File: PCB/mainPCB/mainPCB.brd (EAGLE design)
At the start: 98.7 x 80 mm, 58 parts, among them CN1 SDS-50J, CN2 SDS-50J, CN3 SDS-50J, CN4 SDS-50J, J2 RASPBERRYPI-40-PIN-GPIO, T2 BC817, T3 BC817, T4 BC817, T6 BC817, U1 AT24C256C-SSHL-B, U11 SFH615A-07, U12 ALQ105, U3 SFH615A-07, U4 ALQ105, U5 SFH615A-07, U6 ALQ105, U7 SFH615A-07, U8 ALQ105

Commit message: Adding files for v0.2
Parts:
- removed J1, J3, J4, J5: (no value), SparkFun-Connectors:1X02_2.54_SCREWTERM
- removed U$1: MCP3208I/SL, adcLib:SO-16DW
- added C10, C11, C2, C3, C4, C5, C6, C7, C8, C9: 0.1uF, SparkFun-Capacitors:0603-CAP
- added C12, C13: 10uF, SparkFun-Capacitors:1206-CAP
- added C14, C15: EEE-HA1C471UPCAP_PAN_EEE_F-L, EEE-HA1C471UP:CAP_PAN_EEE_F-L
- added CN5, CN6, CN7, CN8: SDS-50J, SDS-50J:SDS-50J
- added CON1: 1776244-4, lib:1776244-4
- added D10, D11, D5, D8, D9: (no value), SparkFun-DiscreteSemi:SMA-DIODE
- added F5, F6, F7, F8: 3544-2, lib:3544-2
- added FRAME3: FRAME-LETTER, SparkFun-Aesthetics:CREATIVE_COMMONS
- added Q1: DMMT5401-7-F, DMMT5401-7-F:SOT26
- added R24: 0, SparkFun-Passives:1206
- added R25, R40, R43, R46, R49: 10k, SparkFun-Passives:0603-RES
- added R26, R41, R44, R47, R50: 47k, SparkFun-Passives:0603-RES
- added R27: DNP, SparkFun-Passives:1206
- added R28, R29, R30, R31, R32, R33, R34, R35: 330, SparkFun-Passives:0603-RES
- added R39, R42, R45, R48: 47, SparkFun-Passives:0603-RES
- added T5, T7, T8, T9: BC817, lib:BC817
- added U$2: MCP3208T-CI/SL, MCP3208T-CI_SL:SOIC16-N_MC
- added U13, U15, U17, U19: SFH615A-07, lib:SFH615A-07
- added U14, U16, U18, U20: ALQ105, lib:ALQ105
- added U2: DMG2305UX-13SOT-23-M, DMG2359UX:SOT-23-M
- R14, R15: device SparkFun-Passives:0603-RES -> SparkFun-Passives:1206
- R21: value 1k -> 3.9k
- moved FRAME2 73.1 mm to (171.1, 3.12)
- moved FRAME1 67.6 mm to (165.7, 3.12)
- moved R20 54.6 mm to (93.4, 11.8), turned to 270 degrees
- moved R14 44.5 mm to (112.8, 2.92), flipped to the top, turned to 180 degrees
- moved R19 34.3 mm to (76.5, 12.6)
- moved U12 18.3 mm to (77.5, 54.6)
- moved U6 17.4 mm to (54.6, 54.6)
- moved U8 16.6 mm to (31.8, 54.6)
- moved U4 15.9 mm to (8.89, 54.6)
- moved R15 13.7 mm to (58.0, 17.0), turned to 270 degrees
- moved R2 13.3 mm to (39.9, 25.9)
- moved R7 13.1 mm to (47.8, 26.6)
- moved R1 13.0 mm to (37.0, 27.8)
- moved R13 12.8 mm to (34.0, 29.7)
- moved R23 11.3 mm to (10.1, 26.8)
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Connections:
- new net 5V_RPI: C12.1, C13.1, Q1.6, R14.1, R27.1, U2.3
- new net A1_F: C2.1, CN1.2, R28.2
- new net A2_F: C3.1, CN2.2, R29.2
- new net A3_F: C4.1, CN3.2, R30.2
- new net A4_F: C5.1, CN4.2, R31.2
- new net A5_F: C6.1, CN5.2, R32.2
- new net A6_F: C7.1, CN6.2, R33.2
- new net A7_F: C8.1, CN7.2, R34.2
- new net A8_F: C9.1, CN8.2, R35.2
- new net N$29: Q1.4, R26.2, U2.1
- new net N$30: CON1.4, D5.A
- new net N$31: F5.P$1, F5.P$2, U14.P$3
- new net N$32: F6.P$1, F6.P$2, U16.P$3
- new net N$33: F7.P$1, F7.P$2, U20.P$3
- new net N$34: F8.P$1, F8.P$2, U18.P$3
- new net N$35: R39.2, U13.P$1
- new net N$36: C10.1, C11.1, R19.1, U$2.15, U$2.16
- new net N$37: R40.2, U13.P$3
- new net N$38: R40.1, R41.2, T5.P$2
- new net N$39: D8.A, T5.P$1, U14.P$2
- new net N$40: R42.2, U15.P$1
- new net N$41: R43.2, U15.P$3
- new net N$42: R43.1, R44.2, T7.P$2
- new net N$43: D9.A, T7.P$1, U16.P$2
- new net N$44: R45.2, U17.P$1
- new net N$45: R46.2, U17.P$3
- new net N$46: R46.1, R47.2, T8.P$2
- new net N$47: D10.A, T8.P$1, U18.P$2
- new net N$48: R48.2, U19.P$1
- new net N$49: R49.2, U19.P$3
- new net N$50: R49.1, R50.2, T9.P$2
- new net N$51: D11.A, T9.P$1, U20.P$2
- new net R5: CN5.5, U14.P$4
- new net R6: CN6.5, U16.P$4
- new net R7: CN7.5, U20.P$4
- new net R8: CN8.5, U18.P$4
- new net RELAY5: J2.13, R39.1
- new net RELAY6: J2.15, R42.1
- new net RELAY7: J2.29, R48.1
- new net RELAY8: J2.31, R45.1
- net 12V: now also D5.C, F5.P$3, F5.P$4, F6.P$3, F6.P$4, F7.P$3, F7.P$4, F8.P$3, F8.P$4; no longer J4.P1, J4.P2
- net 3_3V: no longer J1.P1, J1.P2, U$1.15
- net 5V: now also C14.1, C15.1, CN5.1, CN6.1, CN7.1, CN8.1, CON1.1, D10.C, D11.C, D8.C, D9.C, Q1.5, R27.2, U12.P$1, U13.P$4, U14.P$1, U15.P$4, U16.P$1, U17.P$4, U18.P$1, U19.P$4, U2.2, U20.P$1, U4.P$1, U6.P$1, U8.P$1; no longer J3.P1, J3.P2, R14.1, U12.P$2, U4.P$2, U6.P$2, U8.P$2
- net A1: now also R28.1, U$2.1; no longer CN1.2, U$1.1
- net A2: now also R29.1, U$2.2; no longer CN2.2, U$1.2
- net A3: now also R30.1, U$2.3; no longer CN3.2, U$1.3
- net A4: now also R31.1, U$2.4; no longer CN4.2, U$1.4
- net A5: now also R32.1, U$2.5; no longer U$1.5
- net A6: now also R33.1, U$2.6; no longer U$1.6
- net A7: now also R34.1, U$2.7; no longer U$1.7
- net A8: now also R35.1, U$2.8; no longer U$1.8
- net AGND: now also U$2.14; no longer U$1.14
- net CLK: now also U$2.13; no longer U$1.13
- net COM: now also CN5.3, CN6.3, CN7.3, CN8.3, R24.1
- net CS_ADC: now also U$2.10; no longer U$1.10
- net GND: now also C10.2, C11.2, C12.2, C13.2, C14.2, C15.2, C2.2, C3.2, C4.2, C5.2, C6.2, C7.2, C8.2, C9.2, CN5.4, CN6.4, CN7.4, CN8.4, CON1.2, CON1.3, R24.2, R25.1, R26.1, R41.1, R44.1, R47.1, R50.1, T5.P$3, T7.P$3, T8.P$3, T9.P$3, U$2.9, U13.P$2, U15.P$2, U17.P$2, U19.P$2; no longer J5.P1, J5.P2, U$1.9
- net MISO: now also U$2.12; no longer U$1.12
- net MOSI: now also U$2.11; no longer U$1.11
- net N$12: now also U6.P$2; no longer U6.P$1
- net N$16: now also U8.P$2; no longer U8.P$1
- net N$24: now also U12.P$2; no longer U12.P$1
- net N$27: now also Q1.1, Q1.2, Q1.3, R25.2; no longer R19.1, U$1.16
- net N$8: now also U4.P$2; no longer U4.P$1
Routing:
- net 5V: track 314.2 -> 578.8 mm
- net RELAY8: track 0.00 -> 168.2 mm, vias 0 -> 3
- net A8_F: track 0.00 -> 150.4 mm
- net COM: track 86.5 -> 230.3 mm
- net RELAY7: track 0.00 -> 139.7 mm, vias 0 -> 3
- net A7_F: track 0.00 -> 133.3 mm
- net GND: track 208.1 -> 78.9 mm, vias 9 -> 78
- net A1_F: track 0.00 -> 114.3 mm
- net A6_F: track 0.00 -> 104.7 mm
- net 12V: track 141.7 -> 233.5 mm
- net A2_F: track 0.00 -> 91.1 mm
- net RELAY6: track 0.00 -> 90.9 mm, vias 0 -> 1
- net A5_F: track 0.00 -> 81.2 mm
- net A1: track 80.4 -> 3.69 mm
- net A3_F: track 0.00 -> 74.4 mm
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- removed copper zone on layer 16, net AGND
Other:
- board size 98.7 x 80 mm -> 187 x 85 mm
- board text added: "v0.2"
- board text removed: "3.3V"
- board text removed: "v0.1"

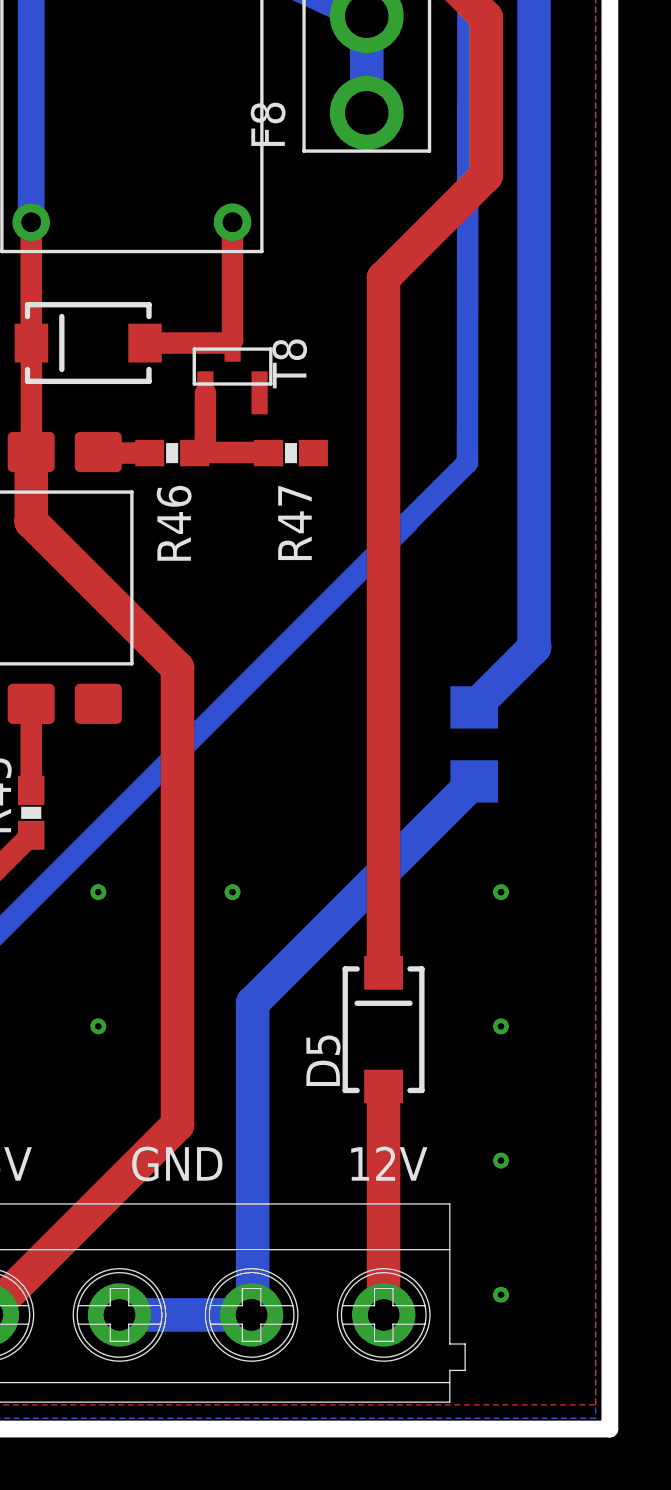
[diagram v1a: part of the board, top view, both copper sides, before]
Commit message: Removed Diode.
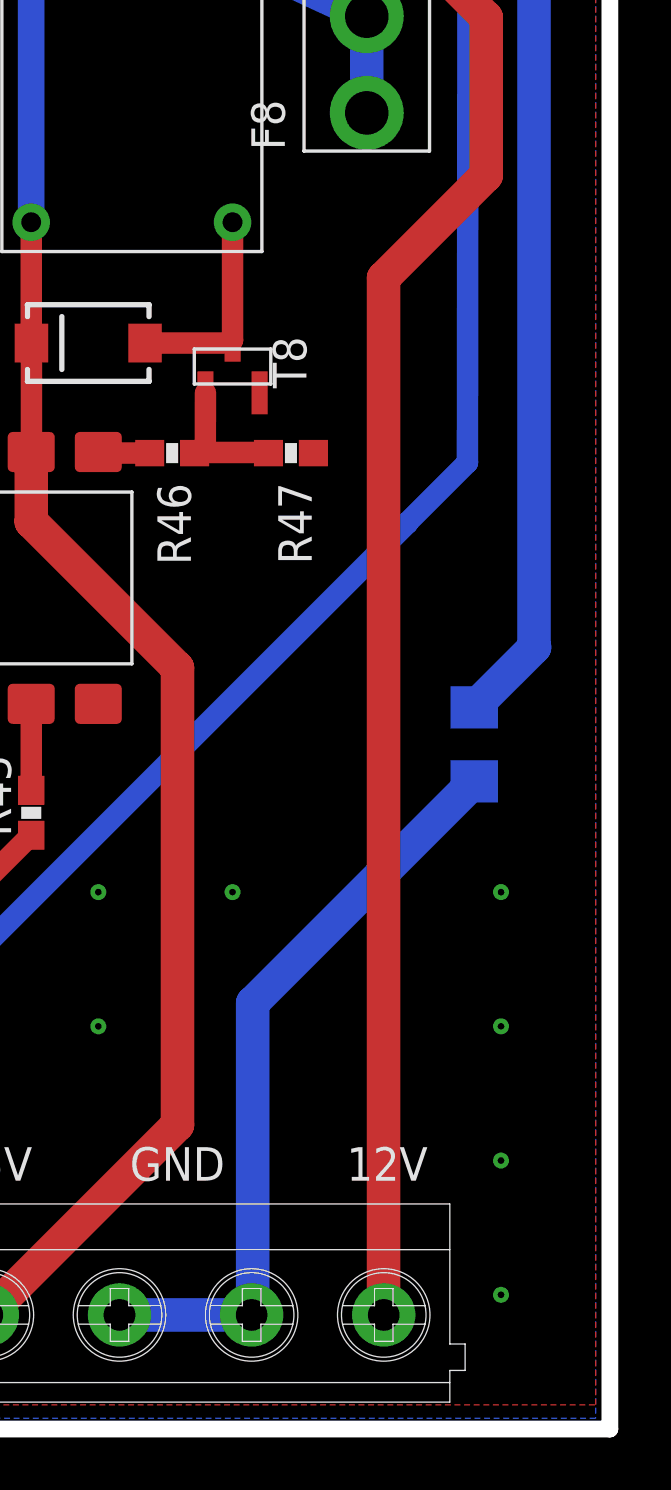
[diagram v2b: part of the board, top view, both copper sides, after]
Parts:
- removed D5: (no value), SparkFun-DiscreteSemi:SMA-DIODE
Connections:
- removed net N$30: CON1.4, D5.A
- net 12V: now also CON1.4; no longer D5.C
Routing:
- net 12V: track 233.5 -> 246.4 mm
- net N$30: track 8.65 -> 0.00 mm
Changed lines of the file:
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@@
 <?xml version="1.0" encoding="utf-8"?>
 <!DOCTYPE eagle SYSTEM "eagle.dtd">
-<eagle version="8.4.3">
+<eagle version="8.3.2">
 <drawing>
 <settings>
@@
 <setting verticaltext="up"/>
 </settings>
-<grid distance="0.127" unitdist="mm" unit="mm" style="dots" multiple="1" display="yes" altdistance="0.127" altunitdist="mm" altunit="mm"/>
+<grid distance="0.127" unitdist="mm" unit="mil" style="dots" multiple="1" display="yes" altdistance="0.127" altunitdist="mm" altunit="mil"/>
 <layers>
 <layer number="1" name="Top" color="4" fill="1" visible="yes" active="yes"/>
@@
 <param name="dpMaxLengthDifference" value="10mm"/>
 <param name="dpGapFactor" value="2.5"/>
+<param name="checkGrid" value="0"/>
 <param name="checkAngle" value="0"/>
 <param name="checkFont" value="1"/>
 <param name="checkRestrict" value="1"/>
-<param name="checkStop" value="0"/>
 <param name="useDiameter" value="13"/>
 <param name="maxErrors" value="50"/>
@@
 <attribute name="NAME" x="97.536" y="18.288" size="1.27" layer="26" font="vector" rot="MR180"/>
 <attribute name="PROD_ID" value="CAP-00810" x="95.885" y="17.78" size="1.778" layer="28" rot="MR180" display="off"/>
-</element>
-<element name="D5" library="SparkFun-DiscreteSemi" package="SMA-DIODE" value="" x="178.435" y="15.113" smashed="yes" rot="R90">
-<attribute name="NAME" x="176.784" y="12.827" size="1.27" layer="25" rot="R90"/>
-<attribute name="VALUE" x="176.784" y="15.367" size="0.4064" layer="27" rot="R90"/>
 </element>
 <element name="FRAME3" library="SparkFun-Aesthetics" package="CREATIVE_COMMONS" value="FRAME-LETTER" x="176.276" y="3.1242" smashed="yes"/>
@@
 <contactref element="F4" pad="P$4"/>
 <contactref element="F4" pad="P$3"/>
-<contactref element="D5" pad="C"/>
 <contactref element="F5" pad="P$4"/>
 <contactref element="F5" pad="P$3"/>
@@
 <wire x1="63.5" y1="57.94" x2="63.5" y2="61.6" width="1.27" layer="1"/>
 <wire x1="182.3212" y1="53.4188" x2="177.8" y2="57.94" width="1.27" layer="1"/>
-<wire x1="178.435" y1="17.263" x2="178.435" y2="43.561" width="1.27" layer="1"/>
-<wire x1="178.435" y1="43.561" x2="182.3212" y2="47.4472" width="1.27" layer="1"/>
+<wire x1="182.3212" y1="47.4472" x2="178.435" y2="43.561" width="1.27" layer="1"/>
 <wire x1="182.3212" y1="47.4472" x2="182.3212" y2="53.4188" width="1.27" layer="1"/>
+<contactref element="CON1" pad="4"/>
+<wire x1="178.435" y1="4.325" x2="178.442" y2="4.318" width="1.27" layer="1"/>
+<wire x1="178.435" y1="43.561" x2="178.435" y2="4.325" width="1.27" layer="1"/>
 </signal>
 <signal name="3.3V">
@@
 <wire x1="23.241" y1="60.833" x2="23.241" y2="40.1574" width="0.8128" layer="16"/>
 </signal>
-<signal name="N$30">
-<contactref element="CON1" pad="4"/>
-<contactref element="D5" pad="A"/>
-<wire x1="178.435" y1="12.963" x2="178.435" y2="4.325" width="1.27" layer="1"/>
-<wire x1="178.435" y1="4.325" x2="178.442" y2="4.318" width="1.27" layer="1"/>
-</signal>
 <signal name="5V_RPI" class="3">

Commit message: Adding files
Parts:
- added D1, D12, D13, D14, D15, D16, D5, D7: BAV99-7-F, SparkFun-DiscreteSemi:SOT23-3
- added F9: 3544-2, lib:3544-2
- moved R24 6.25 mm to (184.2, 31.7)
- moved C14 1.27 mm to (147.4, 13.8)
- moved C15 1.27 mm to (158.9, 13.8)
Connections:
- new net N$28: CON1.4, F9.P$1, F9.P$2
- net 12V: now also F9.P$3, F9.P$4; no longer CON1.4
- net 5V: now also D1.2, D12.2, D13.2, D14.2, D15.2, D16.2, D5.2, D7.2
- net A1_F: now also D1.3
- net A2_F: now also D5.3
- net A3_F: now also D7.3
- net A4_F: now also D12.3
- net A5_F: now also D13.3
- net A6_F: now also D14.3
- net A7_F: now also D15.3
- net A8_F: now also D16.3
- net GND: now also D1.1, D12.1, D13.1, D14.1, D15.1, D16.1, D5.1, D7.1
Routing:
- net 5V: track 578.8 -> 684.3 mm, vias 1 -> 8
- net 12V: track 246.4 -> 230.5 mm
- net N$28: track 0.00 -> 11.4 mm
- net GND: track 78.9 -> 88.0 mm, vias 78 -> 86
- net COM: track 230.3 -> 223.5 mm
- net A6_F: track 104.7 -> 105.5 mm
- net A7_F: track 133.3 -> 133.9 mm
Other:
- board text added: "v0.3"
- board text removed: "v0.2"

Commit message: Technically version 0.4. Sending it to JLCPCB for production.
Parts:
- removed CON1: 1776244-4, lib:1776244-4
- added J1: 1935161, 1935161:PHOENIX_1935161
- added L1: DR73-1R0-R, DR73-1R0-R:DR73
- added R36: 0, SparkFun-Passives:1206
- added TP_ON/OFF, TP_TRIM: TEST-POINT3X5, SparkFun-Passives:PAD.03X.05
- added U9: S24SE05004PDFA, S24SE05004PDFA:CONV_S24SE05002PDFA
- C12, C13: value 10uF -> 1uF
- moved R25 28.4 mm to (112.6, 23.5), turned to 270 degrees
- moved Q1 27.1 mm to (114.0, 18.1), turned to 0 degrees
- moved R26 24.1 mm to (115.7, 23.5), turned to 270 degrees
- moved C14 20.6 mm to (167.5, 18.8)
- moved U2 19.6 mm to (118.6, 19.2), turned to 270 degrees
- moved R24 18.4 mm to (185.3, 13.3)
- moved R27 16.6 mm to (122.7, 19.0), turned to 270 degrees
- moved R48 15.0 mm to (130.4, 32.5)
- moved R42 14.4 mm to (107.3, 31.2)
- moved C15 11.3 mm to (167.5, 6.53), turned to 270 degrees
- moved F9 8.75 mm to (176.5, 9.42)
- moved R45 8.72 mm to (157.4, 27.4), turned to 0 degrees
- moved C12 7.77 mm to (113.9, 4.32)
- moved R14 7.11 mm to (105.7, 2.92)
- moved U15 6.98 mm to (114.6, 35.7), turned to 0 degrees
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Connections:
- removed net N$28: CON1.4, F9.P$1, F9.P$2
- new net N$30: TP_ON/OFF.P$1, U9.3
- new net N$52: L1.1, U9.1
- new net N$53: TP_TRIM.P$1, U9.5
- new net N$54: F9.P$1, F9.P$2, J1.1
- net 12V: now also C14.1, C15.1, L1.2
- net 5V: now also Q1.6, R27.1, U2.3, U9.6; no longer C14.1, C15.1, CON1.1, Q1.5, R27.2, U2.2
- net 5V_RPI: now also Q1.5, R27.2, U2.2; no longer Q1.6, R27.1, U2.3
- net COM: now also R36.1
- net GND: now also J1.2, R36.2, U9.2, U9.4; no longer CON1.2, CON1.3
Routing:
- net 5V: track 684.3 -> 770.4 mm
- net 12V: track 230.5 -> 189.3 mm
- net COM: track 223.5 -> 182.6 mm
- net GND: track 88.0 -> 54.9 mm, vias 86 -> 131
- net N$54: track 0.00 -> 12.0 mm
- net N$28: track 11.4 -> 0.00 mm
- net RELAY7: track 139.7 -> 151.0 mm, vias 3 -> 5
- net N$53: track 0.00 -> 8.80 mm
- net N$30: track 0.00 -> 6.76 mm
- net N$17: track 57.1 -> 50.7 mm
- net A7_F: track 133.9 -> 129.2 mm
- net N$41: track 2.33 -> 5.93 mm
- net N$44: track 3.27 -> 6.87 mm
- net A8_F: track 150.6 -> 147.1 mm
- net N$49: track 2.34 -> 5.76 mm
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- added copper zone on layer 1, net 12V
- added copper zone on layer 1, net 5V
- added copper zone on layer 1, net 5V_RPI
- added copper zone on layer 16, net COM
- added copper zone on layer 1, net N$52
- added copper zone on layer 1, net N$54
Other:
- board size 187 x 85 mm -> 197 x 87 mm
- board text added: "Danger - Shock Hazard!"
- board text added: "Designed by Diego Aguilera for Very."
- board text added: "HOP"
- board text added: "Jumper to program EEPROM"
- board text added: "PCB v0.4"
- board text removed: "5V"
- board text removed: "v0.3"
